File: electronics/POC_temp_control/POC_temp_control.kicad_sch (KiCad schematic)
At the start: 206 parts, among them J1 Conn_01x02, J2 Conn_01x07, J3 Conn_01x05, J4 Conn_01x06, J5 Conn_01x04, J6 Conn_01x06, Q1 PXT8050, Q10 BC847A, Q11 BC858B, Q12 BC847A, Q2 PXT8050, Q3 PXT8550, Q4 DMP6050SSD, Q5 DMP6050SSD, Q6 BC858B, Q7 BC858B, Q8 BC847A, Q9 BC847A, T1 10P_1P_2S, U1 SY8120, U10 BL24C02F, U2 MCP1702T-3302, U4 LM358, U5 OP07, U6 OP07, U7 OP07, U8 74XX4051, U9 74XX4051

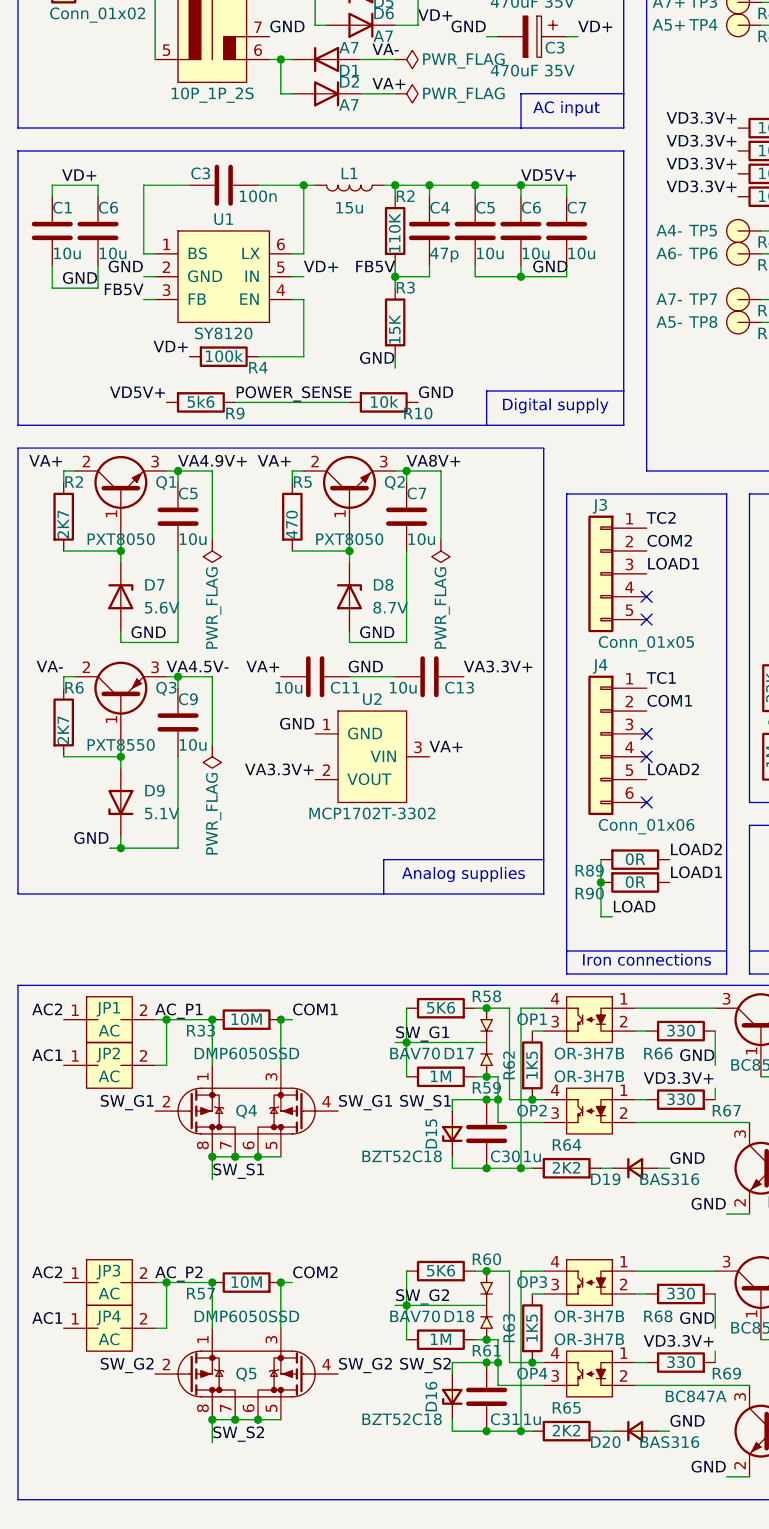
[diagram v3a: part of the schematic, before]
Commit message: Updated PCB/Schematic to kicad 9
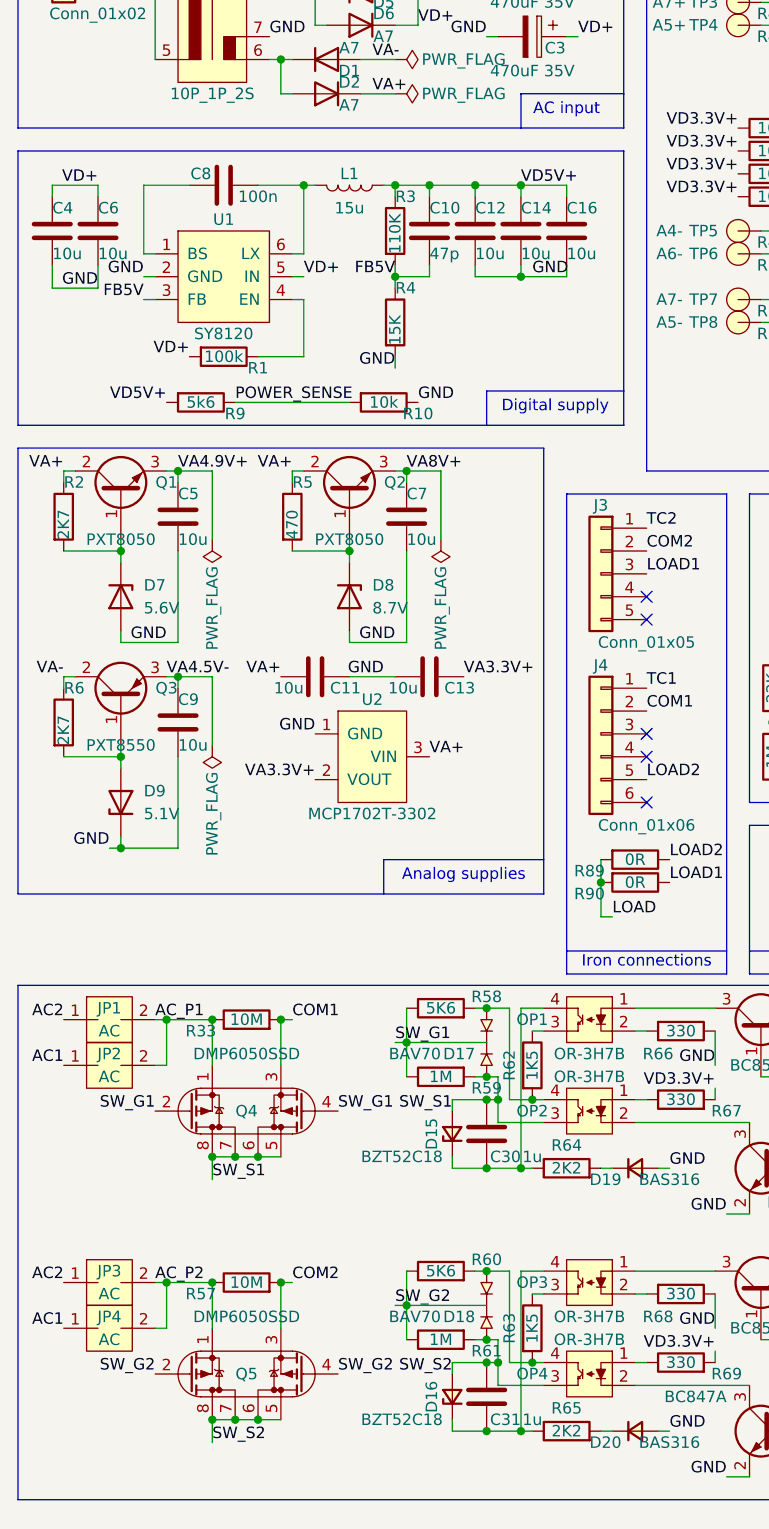
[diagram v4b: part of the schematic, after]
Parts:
- renumbered C4 to C10, C5 to C12, C6 to C14, C7 to C16, C1 to C4, C3 to C8, R4 to R1, R2 to R3, R3 to R4
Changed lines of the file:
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@@
 (kicad_sch
-	(version 20231120)
+	(version 20250114)
 	(generator "eeschema")
-	(generator_version "8.0")
+	(generator_version "9.0")
 	(paper "A4")
+	(text "filtered signals"
+		(exclude_from_sim no)
+		(at 273.05 107.95 0)
+		(effects
+			(font
+				(size 1.27 1.27)
+			)
+			(justify bottom)
+		)
+	)
+	(text "AC input"
+		(exclude_from_sim no)
+		(at 74.93 41.91 0)
+		(effects
+			(font
+				(size 1.27 1.27)
+			)
+			(justify bottom)
+		)
+	)
+	(text "Analog supplies"
+		(exclude_from_sim no)
+		(at 63.5 127 0)
+		(effects
+			(font
+				(size 1.27 1.27)
+			)
+			(justify bottom)
+		)
+	)
+	(text "Power switches"
+		(exclude_from_sim no)
+		(at 106.68 194.31 0)
+		(effects
+			(font
+				(size 1.27 1.27)
+			)
+			(justify bottom)
+		)
+	)
+	(text "Digital supply"
+		(exclude_from_sim no)
+		(at 73.66 74.93 0)
+		(effects
+			(font
+				(size 1.27 1.27)
+			)
+			(justify bottom)
+		)
+	)
+	(text "Power control leds"
+		(exclude_from_sim no)
+		(at 241.3 163.83 0)
+		(effects
+			(font
+				(size 1.27 1.27)
+			)
+		)
+	)
+	(text "Logos and version"
+		(exclude_from_sim no)
+		(at 105.41 135.89 0)
+		(effects
+			(font
+				(size 1.27 1.27)
+			)
+		)
+	)
+	(text "I2C EEPROM"
+		(exclude_from_sim no)
+		(at 276.86 163.83 0)
+		(effects
+			(font
+				(size 1.27 1.27)
+			)
+		)
+	)
+	(text "Signal muxes"
+		(exclude_from_sim no)
+		(at 140.97 80.01 0)
+		(effects
+			(font
+				(size 1.27 1.27)
+			)
+			(justify bottom)
+		)
+	)
+	(text "Zerocross"
+		(exclude_from_sim no)
+		(at 125.73 116.84 0)
+		(effects
+			(font
+				(size 1.27 1.27)
+			)
+		)
+	)
+	(text "Case stuff"
+		(exclude_from_sim no)
+		(at 147.32 195.58 0)
+		(effects
+			(font
+				(size 1.27 1.27)
+			)
+		)
+	)
+	(text "Power in"
+		(exclude_from_sim no)
+		(at 139.7 100.33 0)
+		(effects
+			(font
+				(size 1.27 1.27)
+			)
+		)
+	)
+	(text "I2C connector"
+		(exclude_from_sim no)
+		(at 140.97 125.73 0)
+		(effects
+			(font
+				(size 1.27 1.27)
+			)
+		)
+	)
+	(text "Differential amplifiers"
+		(exclude_from_sim no)
+		(at 201.93 107.95 0)
+		(effects
+			(font
+				(size 1.27 1.27)
+			)
+			(justify top)
+		)
+	)
+	(text "Iron connections"
+		(exclude_from_sim no)
+		(at 83.82 135.89 0)
+		(effects
+			(font
+				(size 1.27 1.27)
+			)
+		)
+	)
+	(text "Power Debug"
+		(exclude_from_sim no)
+		(at 243.84 139.7 0)
+		(effects
+			(font
+				(size 1.27 1.27)
+			)
+			(justify bottom)
+		)
+	)
+	(text "post amplifiers"
+		(exclude_from_sim no)
+		(at 212.09 34.29 0)
+		(effects
+			(font
+				(size 1.27 1.27)
+			)
+			(justify bottom)
+		)
+	)
+	(text "TODO"
+		(exclude_from_sim no)
+		(at 172.72 195.58 0)
+		(effects
+			(font
+				(size 1.27 1.27)
+			)
+		)
+	)
+	(text "Nuclone"
+		(exclude_from_sim no)
+		(at 278.13 78.74 0)
+		(effects
+			(font
+				(size 1.27 1.27)
+			)
+			(justify bottom)
+		)
+	)
+	(text "sensing resistors"
+		(exclude_from_sim no)
+		(at 273.05 138.43 0)
+		(effects
+			(font
+				(size 1.27 1.27)
+			)
+		)
+	)
 	(junction
 		(at 59.69 49.53)
@@
 		)
 	)
-	(text "filtered signals"
-		(exclude_from_sim no)
-		(at 273.05 107.95 0)
-		(effects
-			(font
-				(size 1.27 1.27)
-			)
-			(justify bottom)
-		)
-	)
-	(text "AC input"
-		(exclude_from_sim no)
-		(at 74.93 41.91 0)
-		(effects
-			(font
-				(size 1.27 1.27)
-			)
-			(justify bottom)
-		)
-	)
-	(text "Analog supplies"
-		(exclude_from_sim no)
-		(at 63.5 127 0)
-		(effects
-			(font
-				(size 1.27 1.27)
-			)
-			(justify bottom)
-		)
-	)
-	(text "Power switches"
-		(exclude_from_sim no)
-		(at 106.68 194.31 0)
-		(effects
-			(font
-				(size 1.27 1.27)
-			)
-			(justify bottom)
-		)
-	)
-	(text "Digital supply"
-		(exclude_from_sim no)
-		(at 73.66 74.93 0)
-		(effects
-			(font
-				(size 1.27 1.27)
-			)
-			(justify bottom)
-		)
-	)
-	(text "Power control leds"
-		(exclude_from_sim no)
-		(at 241.3 163.83 0)
-		(effects
-			(font
-				(size 1.27 1.27)
-			)
-		)
-	)
-	(text "Logos and version"
-		(exclude_from_sim no)
-		(at 105.41 135.89 0)
-		(effects
-			(font
-				(size 1.27 1.27)
-			)
-		)
-	)
-	(text "I2C EEPROM"
-		(exclude_from_sim no)
-		(at 276.86 163.83 0)
-		(effects
-			(font
-				(size 1.27 1.27)
-			)
-		)
-	)
-	(text "Signal muxes"
-		(exclude_from_sim no)
-		(at 140.97 80.01 0)
-		(effects
-			(font
-				(size 1.27 1.27)
-			)
-			(justify bottom)
-		)
-	)
-	(text "Zerocross"
-		(exclude_from_sim no)
-		(at 125.73 116.84 0)
-		(effects
-			(font
-				(size 1.27 1.27)
-			)
-		)
-	)
-	(text "Case stuff"
-		(exclude_from_sim no)
-		(at 147.32 195.58 0)
-		(effects
-			(font
-				(size 1.27 1.27)
-			)
-		)
-	)
-	(text "Power in"
-		(exclude_from_sim no)
-		(at 139.7 100.33 0)
-		(effects
-			(font
-				(size 1.27 1.27)
-			)
-		)
-	)
-	(text "I2C connector"
-		(exclude_from_sim no)
-		(at 140.97 125.73 0)
-		(effects
-			(font
-				(size 1.27 1.27)
-			)
-		)
-	)
-	(text "Differential amplifiers"
-		(exclude_from_sim no)
-		(at 201.93 107.95 0)
-		(effects
-			(font
-				(size 1.27 1.27)
-			)
-			(justify top)
-		)
-	)
-	(text "Iron connections"
-		(exclude_from_sim no)
-		(at 83.82 135.89 0)
-		(effects
-			(font
-				(size 1.27 1.27)
-			)
-		)
-	)
-	(text "Power Debug"
-		(exclude_from_sim no)
-		(at 243.84 139.7 0)
-		(effects
-			(font
-				(size 1.27 1.27)
-			)
-			(justify bottom)
-		)
-	)
-	(text "post amplifiers"
-		(exclude_from_sim no)
-		(at 212.09 34.29 0)
-		(effects
-			(font
-				(size 1.27 1.27)
-			)
-			(justify bottom)
-		)
-	)
-	(text "TODO"
-		(exclude_from_sim no)
-		(at 172.72 195.58 0)
-		(effects
-			(font
-				(size 1.27 1.27)
-			)
-		)
-	)
-	(text "Nuclone"
-		(exclude_from_sim no)
-		(at 278.13 78.74 0)
-		(effects
-			(font
-				(size 1.27 1.27)
-			)
-			(justify bottom)
-		)
-	)
-	(text "sensing resistors"
-		(exclude_from_sim no)
-		(at 273.05 138.43 0)
-		(effects
-			(font
-				(size 1.27 1.27)
-			)
-		)
-	)
 	(label "TC_FILT"
 		(at 275.59 95.25 0)
@@
 		(on_board yes)
 		(dnp no)
-		(property "Reference" "C3"
+		(property "Reference" "C8"
 			(at 34.29 48.26 90)
 			(effects
@@
 		(on_board yes)
 		(dnp no)
-		(property "Reference" "R2"
+		(property "Reference" "R3"
 			(at 55.88 50.8 0)
 			(effects
@@
 		(on_board yes)
 		(dnp no)
-		(property "Reference" "R3"
+		(property "Reference" "R4"
 			(at 55.88 60.96 0)
 			(effects
@@
 		(on_board yes)
 		(dnp no)
-		(property "Reference" "C4"
+		(property "Reference" "C10"
 			(at 59.69 52.07 0)
 			(effects
@@
 		(on_board yes)
 		(dnp no)
-		(property "Reference" "R4"
+		(property "Reference" "R1"
 			(at 40.64 69.85 90)
 			(effects
@@
 		(on_board yes)
 		(dnp no)
-		(property "Reference" "C1"
+		(property "Reference" "C4"
 			(at 17.78 52.07 0)
 			(effects
@@
 		(on_board yes)
 		(dnp no)
-		(property "Reference" "C6"
+		(property "Reference" "C14"
 			(at 69.85 52.07 0)
 			(effects
@@
 		(on_board yes)
 		(dnp no)
-		(property "Reference" "C5"
+		(property "Reference" "C12"
 			(at 64.77 52.07 0)
 			(effects
@@
 		(on_board yes)
 		(dnp no)
-		(property "Reference" "C7"
+		(property "Reference" "C16"
 			(at 74.93 52.07 0)
 			(effects
@@
 		)
 	)
+	(embedded_fonts no)
 )
